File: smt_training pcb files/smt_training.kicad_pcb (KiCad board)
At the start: 2 copper layers, 100 x 40 mm, 73 parts, among them J1 AU-Y1006-2, Q1 2N7002-7-F, SW1 PTS636SK25FSMTR LFS, SW2 PTS526SM15SMTR2 LFS, U1 SN74LVC1G08DBVR, U2 SN74LVC1G86DCKR, U3 LQFP64 IC, U4 NE555S-13

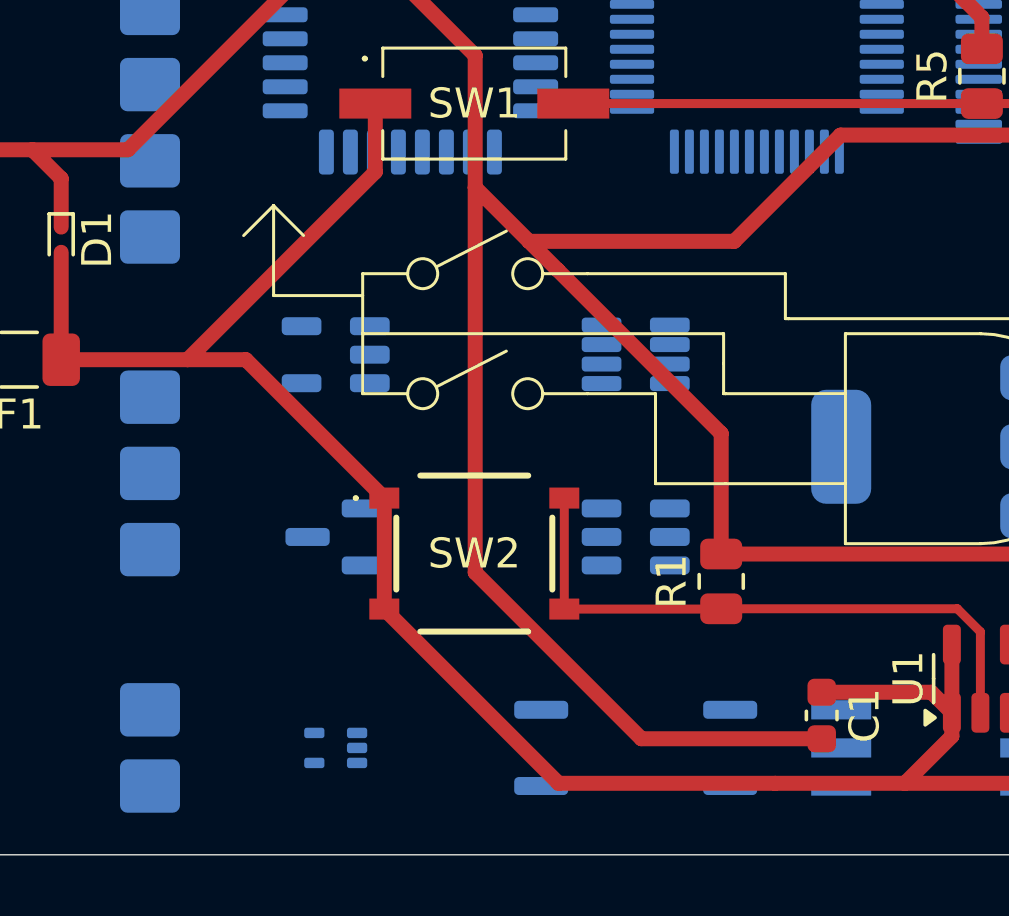
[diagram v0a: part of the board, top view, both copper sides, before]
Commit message: Fixed Bypassed SW2; Added Soldermask to Back Icons; Updated Version Number
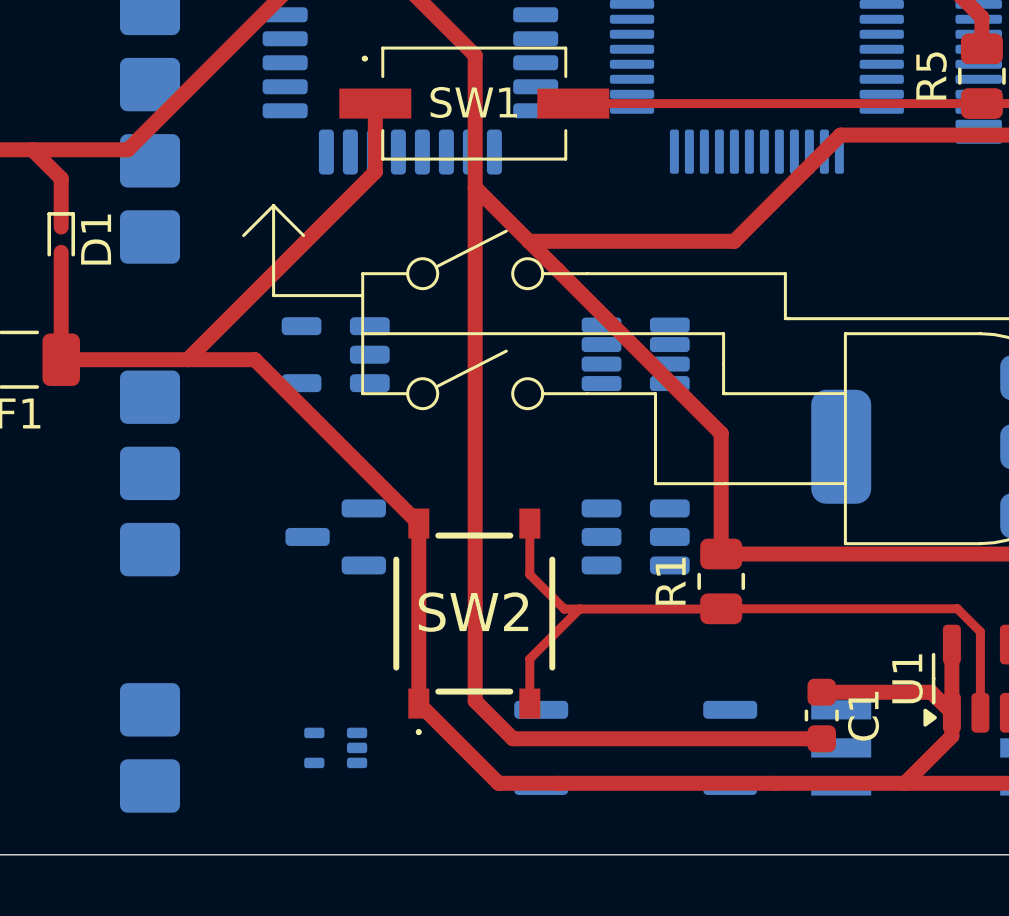
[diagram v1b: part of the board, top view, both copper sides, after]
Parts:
- moved SW2 2.00 mm to (49.9, 69.7), turned to 90 degrees
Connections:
- SW2 pad 2: Net-(R1-Pad1) -> +5V
- SW2 pad 3: +5V -> Net-(R1-Pad1)
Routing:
- net Net-(R1-Pad1): track 20.6 -> 24.1 mm
- net GND: track 273.1 -> 275.6 mm
- net +5V: track 139.7 -> 141.0 mm
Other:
- board text added: "Henry Tejada Deras v1.1 2025-11"
- board text removed: "Henry Tejada Deras v1 2025-10"
